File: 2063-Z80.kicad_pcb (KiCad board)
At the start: 4 copper layers, 100 x 100 mm, 82 parts, among them J1 Conn_01x05, J10 Conn_01x07, J11 Conn_02x03, J12 Conn_01x02, J2 DM3D-SF(41), J3 Conn_02x20, J4 Conn_02x05, J5 Conn_02x05, J6 0548190519, J7 Conn_02x13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

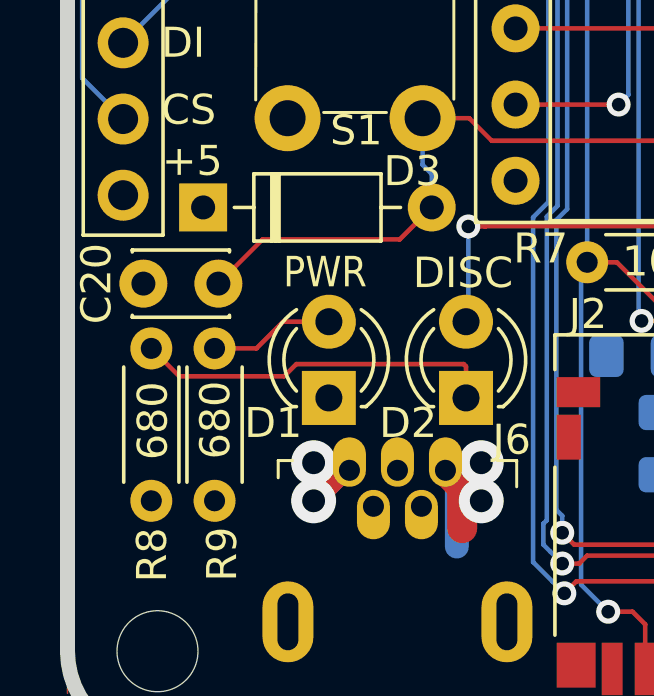
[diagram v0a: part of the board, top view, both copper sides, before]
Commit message: Increase 5V copper to close thru-hole pads
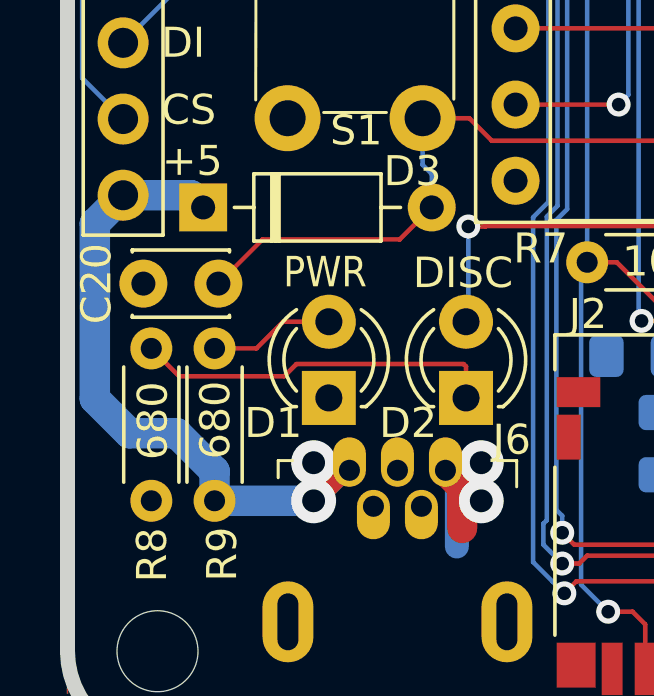
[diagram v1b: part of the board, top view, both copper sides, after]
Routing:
- net +5V: track 21.5 -> 40.8 mm
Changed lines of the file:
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@@
     (thickness 1.6)
     (drawings 111)
-    (tracks 2215)
+    (tracks 2224)
     (zones 0)
     (modules 82)
@@
   (segment (start 120.015 137.087) (end 120.464 136.638) (width 0.762) (layer B.Cu) (net 23))
   (segment (start 120.015 137.16) (end 120.015 137.087) (width 0.762) (layer B.Cu) (net 23))
+  (segment (start 104.902 141.986) (end 108.204 141.986) (width 1.016) (layer B.Cu) (net 23))
+  (segment (start 104.1146 131.8006) (end 104.521 132.207) (width 1.016) (layer B.Cu) (net 23))
+  (segment (start 101.854 131.8006) (end 104.1146 131.8006) (width 1.016) (layer B.Cu) (net 23))
+  (segment (start 100.91041 132.74419) (end 101.854 131.8006) (width 1.016) (layer B.Cu) (net 23))
+  (segment (start 100.91041 138.58369) (end 100.91041 132.74419) (width 1.016) (layer B.Cu) (net 23))
+  (segment (start 102.05974 139.73302) (end 100.91041 138.58369) (width 1.016) (layer B.Cu) (net 23))
+  (segment (start 104.902 140.996051) (end 103.638969 139.73302) (width 1.016) (layer B.Cu) (net 23))
+  (segment (start 103.638969 139.73302) (end 102.05974 139.73302) (width 1.016) (layer B.Cu) (net 23))
+  (segment (start 104.902 141.986) (end 104.902 140.996051) (width 1.016) (layer B.Cu) (net 23))
   (segment (start 105.596081 57.912) (end 106.624682 58.940601) (width 0.1524) (layer F.Cu) (net 24))
   (segment (start 104.394 57.912) (end 105.596081 57.912) (width 0.1524) (layer F.Cu) (net 24))
@@
   (segment (start 154.028039 55.295901) (end 154.76728 54.55666) (width 0.1524) (layer B.Cu) (net 152))
   (zone (net 14) (net_name GND) (layer In1.Cu) (hatch edge 0.508)
-    (connect_pads (clearance 0.2032))
+    (connect_pads yes (clearance 0.2032))
     (min_thickness 0.2032)
     (fill yes (arc_segments 32) (thermal_gap 0.2032) (thermal_bridge_width 0.508))
@@
   )
   (zone (net 23) (net_name +5V) (layer In2.Cu) (hatch edge 0.508)
-    (connect_pads (clearance 0.2032))
+    (connect_pads yes (clearance 0.2032))
     (min_thickness 0.2032)
     (fill yes (arc_segments 32) (thermal_gap 0.2032) (thermal_bridge_width 0.508))

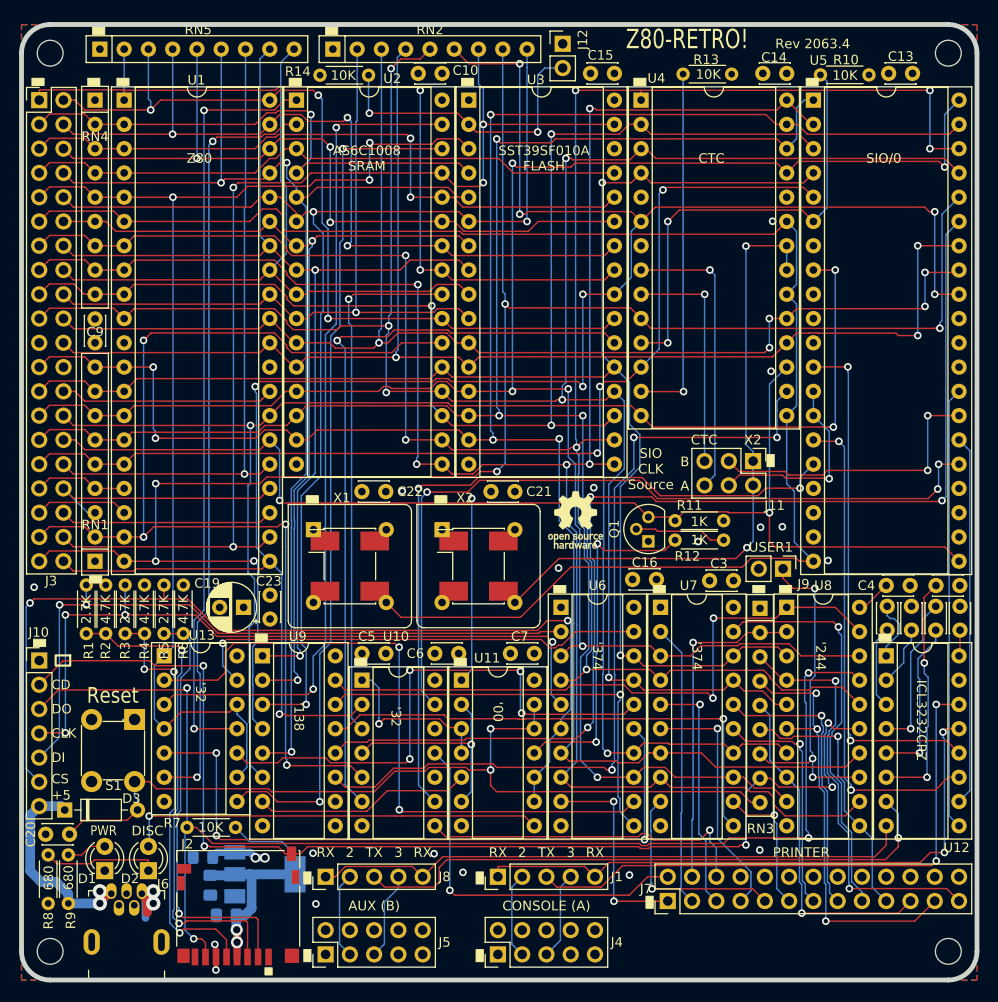
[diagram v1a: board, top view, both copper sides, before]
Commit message: Terminate the clock traces.
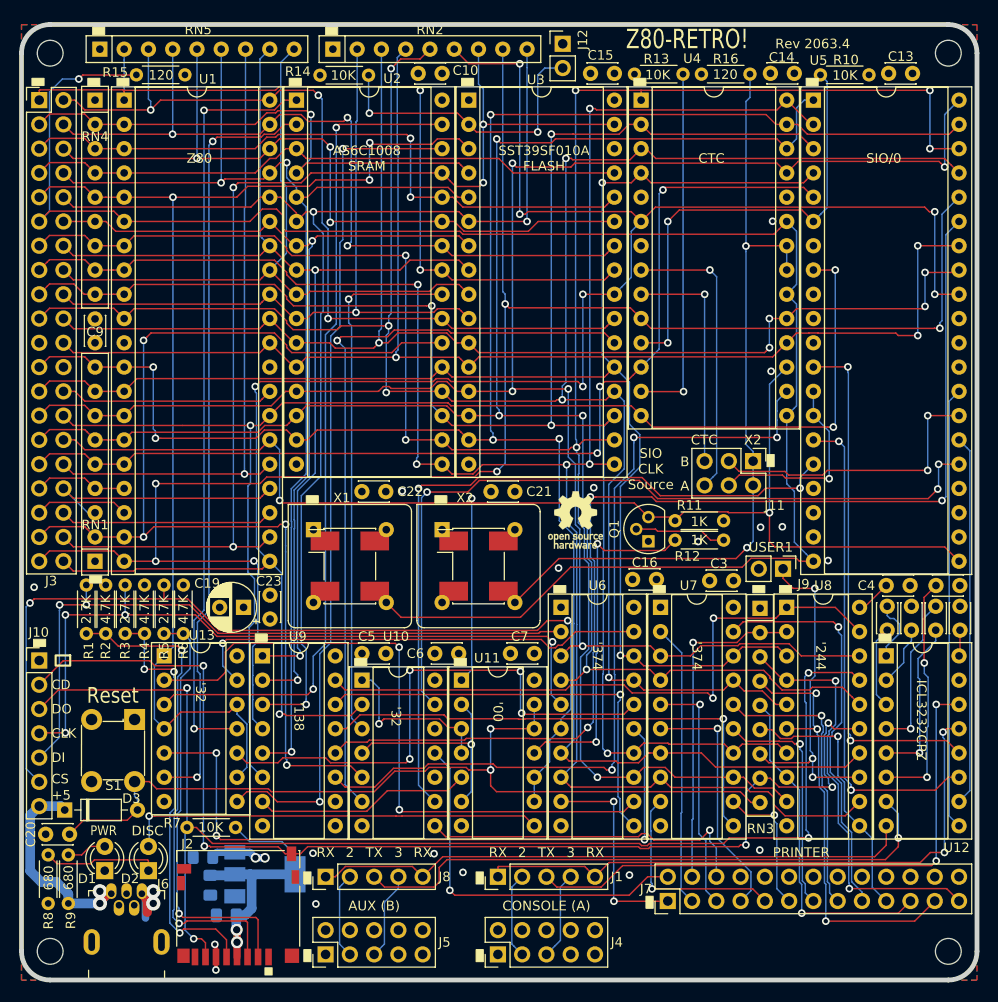
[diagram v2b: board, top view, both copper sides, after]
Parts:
- added R15: 120, Resistor_THT:R_Axial_DIN0204_L3.6mm_D1.6mm_P5.08mm_Horizontal, F.Cu at (117.1, 55.3)
- added R16: 120, Resistor_THT:R_Axial_DIN0204_L3.6mm_D1.6mm_P5.08mm_Horizontal, F.Cu at (171.2, 55.2)
- moved C14 0.80 mm to (180.9, 55.1)
- turned R13 to 180 degrees
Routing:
- net /CLK: track 170.7 -> 194.6 mm, vias 0 -> 1
- net /BAUD_CLK: track 67.3 -> 85.5 mm
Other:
- board text added: "120"

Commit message: Keep more of the main CLK on on front layer
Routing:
- net /CLK: track 194.6 -> 197.4 mm, vias 1 -> 0
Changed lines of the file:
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@@
     (thickness 1.6)
     (drawings 113)
-    (tracks 2235)
+    (tracks 2238)
     (zones 0)
     (modules 84)
@@
   (segment (start 120.015 137.16) (end 120.015 137.087) (width 0.762) (layer B.Cu) (net 23))
   (segment (start 104.902 141.986) (end 108.204 141.986) (width 1.016) (layer B.Cu) (net 23))
-  (segment (start 104.1146 131.8006) (end 104.521 132.207) (width 1.016) (layer B.Cu) (net 23))
-  (segment (start 101.854 131.8006) (end 104.1146 131.8006) (width 1.016) (layer B.Cu) (net 23))
   (segment (start 100.91041 132.74419) (end 101.854 131.8006) (width 1.016) (layer B.Cu) (net 23))
   (segment (start 100.91041 138.58369) (end 100.91041 132.74419) (width 1.016) (layer B.Cu) (net 23))
@@
   (segment (start 103.638969 139.73302) (end 102.05974 139.73302) (width 1.016) (layer B.Cu) (net 23))
   (segment (start 104.902 141.986) (end 104.902 140.996051) (width 1.016) (layer B.Cu) (net 23))
+  (segment (start 104.5083 132.1943) (end 104.521 132.207) (width 1.016) (layer B.Cu) (net 23))
+  (segment (start 103.2764 132.1943) (end 104.5083 132.1943) (width 1.016) (layer B.Cu) (net 23))
+  (segment (start 102.8827 131.8006) (end 103.2764 132.1943) (width 1.016) (layer B.Cu) (net 23))
+  (segment (start 101.854 131.8006) (end 102.8827 131.8006) (width 1.016) (layer B.Cu) (net 23))
   (segment (start 105.596081 57.912) (end 106.624682 58.940601) (width 0.1524) (layer F.Cu) (net 24))
   (segment (start 104.394 57.912) (end 105.596081 57.912) (width 0.1524) (layer F.Cu) (net 24))
@@
   (segment (start 181.102 105.8672) (end 176.3522 105.8672) (width 0.1524) (layer F.Cu) (net 48))
   (segment (start 182.88 106.172) (end 181.4068 106.172) (width 0.1524) (layer F.Cu) (net 48))
-  (segment (start 102.932601 69.533399) (end 102.932601 57.049299) (width 0.1524) (layer B.Cu) (net 48))
-  (segment (start 101.854 70.612) (end 102.932601 69.533399) (width 0.1524) (layer B.Cu) (net 48))
-  (via (at 105.99928 55.7022) (size 0.8) (drill 0.45) (layers F.Cu B.Cu) (net 48))
-  (segment (start 104.2797 55.7022) (end 105.99928 55.7022) (width 0.1524) (layer B.Cu) (net 48))
-  (segment (start 102.932601 57.049299) (end 104.2797 55.7022) (width 0.1524) (layer B.Cu) (net 48))
-  (segment (start 112.00384 55.28818) (end 112.02416 55.26786) (width 0.1524) (layer F.Cu) (net 48))
-  (segment (start 106.4133 55.28818) (end 112.00384 55.28818) (width 0.1524) (layer F.Cu) (net 48))
-  (segment (start 105.99928 55.7022) (end 106.4133 55.28818) (width 0.1524) (layer F.Cu) (net 48))
+  (segment (start 100.47861 69.23661) (end 101.004001 69.762001) (width 0.1524) (layer F.Cu) (net 48))
+  (segment (start 100.47861 56.70421) (end 100.47861 69.23661) (width 0.1524) (layer F.Cu) (net 48))
+  (segment (start 101.16566 56.01716) (end 100.47861 56.70421) (width 0.1524) (layer F.Cu) (net 48))
+  (segment (start 105.68432 56.01716) (end 101.16566 56.01716) (width 0.1524) (layer F.Cu) (net 48))
+  (segment (start 101.004001 69.762001) (end 101.854 70.612) (width 0.1524) (layer F.Cu) (net 48))
+  (segment (start 106.4133 55.28818) (end 105.68432 56.01716) (width 0.1524) (layer F.Cu) (net 48))
+  (segment (start 112.00384 55.28818) (end 106.4133 55.28818) (width 0.1524) (layer F.Cu) (net 48))
+  (segment (start 112.02416 55.26786) (end 112.00384 55.28818) (width 0.1524) (layer F.Cu) (net 48))
   (segment (start 108.82737 68.072) (end 110.744 68.072) (width 0.1524) (layer F.Cu) (net 49))
   (segment (start 107.696 68.072) (end 108.82737 68.072) (width 0.1524) (layer F.Cu) (net 49))
@@
   (segment (start 166.3446 69.1134) (end 194.531715 69.1134) (width 0.1524) (layer F.Cu) (net 54))
   (segment (start 164.846 70.612) (end 166.3446 69.1134) (width 0.1524) (layer F.Cu) (net 54))
-  (segment (start 101.854 57.912) (end 101.854 56.9096) (width 0.1524) (layer F.Cu) (net 55))
-  (segment (start 101.854 56.9096) (end 101.930201 56.833399) (width 0.1524) (layer F.Cu) (net 55))
-  (segment (start 101.930201 56.833399) (end 110.617799 56.833399) (width 0.1524) (layer F.Cu) (net 55))
-  (segment (start 110.617799 56.833399) (end 110.744 56.9596) (width 0.1524) (layer F.Cu) (net 55))
   (segment (start 110.744 53.70937) (end 110.744 57.912) (width 0.1524) (layer B.Cu) (net 55))
   (segment (start 110.744 52.578) (end 110.744 53.70937) (width 0.1524) (layer B.Cu) (net 55))
@@
   (segment (start 141.732 75.692) (end 144.018 75.692) (width 0.1524) (layer F.Cu) (net 55))
   (segment (start 110.744 57.912) (end 110.744 56.9596) (width 0.1524) (layer F.Cu) (net 55))
-  (segment (start 110.820201 56.883399) (end 126.581535 56.883399) (width 0.1524) (layer F.Cu) (net 55))
+  (segment (start 110.744 56.833399) (end 110.744 56.9596) (width 0.1524) (layer F.Cu) (net 55))
+  (segment (start 101.930201 56.833399) (end 110.744 56.833399) (width 0.1524) (layer F.Cu) (net 55))
+  (segment (start 101.854 56.9096) (end 101.930201 56.833399) (width 0.1524) (layer F.Cu) (net 55))
+  (segment (start 101.854 57.912) (end 101.854 56.9096) (width 0.1524) (layer F.Cu) (net 55))
+  (segment (start 141.332001 56.496001) (end 141.732 56.896) (width 0.1524) (layer F.Cu) (net 55))
   (segment (start 126.581535 56.883399) (end 126.968933 56.496001) (width 0.1524) (layer F.Cu) (net 55))
-  (segment (start 110.744 56.9596) (end 110.820201 56.883399) (width 0.1524) (layer F.Cu) (net 55))
+  (segment (start 110.794 56.883399) (end 126.581535 56.883399) (width 0.1524) (layer F.Cu) (net 55))
   (segment (start 126.968933 56.496001) (end 141.332001 56.496001) (width 0.1524) (layer F.Cu) (net 55))
-  (segment (start 141.332001 56.496001) (end 141.732 56.896) (width 0.1524) (layer F.Cu) (net 55))
+  (segment (start 110.744 56.833399) (end 110.794 56.883399) (width 0.1524) (layer F.Cu) (net 55))
   (via (at 122.555 146.05) (size 1.27) (drill 0.762) (layers F.Cu B.Cu) (net 57))
   (via (at 122.520553 144.74191) (size 1.27) (drill 0.762) (layers F.Cu B.Cu) (net 57))
@@
   (segment (start 198.12 96.012) (end 195.99148 96.012) (width 0.1524) (layer F.Cu) (net 149))
   (via (at 195.89242 98.6155) (size 0.8) (drill 0.45) (layers F.Cu B.Cu) (net 149))
-  (segment (start 195.98386 98.52406) (end 195.89242 98.6155) (width 0.1524) (layer B.Cu) (net 149))
-  (segment (start 195.98386 96.01962) (end 195.98386 98.52406) (width 0.1524) (layer B.Cu) (net 149))
   (segment (start 146.706531 98.933) (end 142.4432 98.933) (width 0.1524) (layer F.Cu) (net 149))
   (segment (start 147.92572 97.713811) (end 146.706531 98.933) (width 0.1524) (layer F.Cu) (net 149))
@@
   (segment (start 194.890008 99.617912) (end 166.572312 99.617912) (width 0.1524) (layer F.Cu) (net 149))
   (segment (start 195.89242 98.6155) (end 194.890008 99.617912) (width 0.1524) (layer F.Cu) (net 149))
+  (segment (start 195.89242 97.88398) (end 195.89242 98.6155) (width 0.1524) (layer B.Cu) (net 149))
+  (segment (start 195.98386 97.79254) (end 195.89242 97.88398) (width 0.1524) (layer B.Cu) (net 149))
+  (segment (start 195.98386 96.01962) (end 195.98386 97.79254) (width 0.1524) (layer B.Cu) (net 149))
   (via (at 136.40816 59.2836) (size 0.8) (drill 0.45) (layers F.Cu B.Cu) (net 152))
   (segment (start 136.3218 59.19724) (end 136.40816 59.2836) (width 0.1524) (layer B.Cu) (net 152))
